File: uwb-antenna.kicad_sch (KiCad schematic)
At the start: 19 parts, among them J1 USB_C_Receptacle_USB2.0_14P, SW1 NRST, SW2 SW_DIP_x02, U1 STM32F401CBUx, Y1 8MHz, Y2 32.768KHz

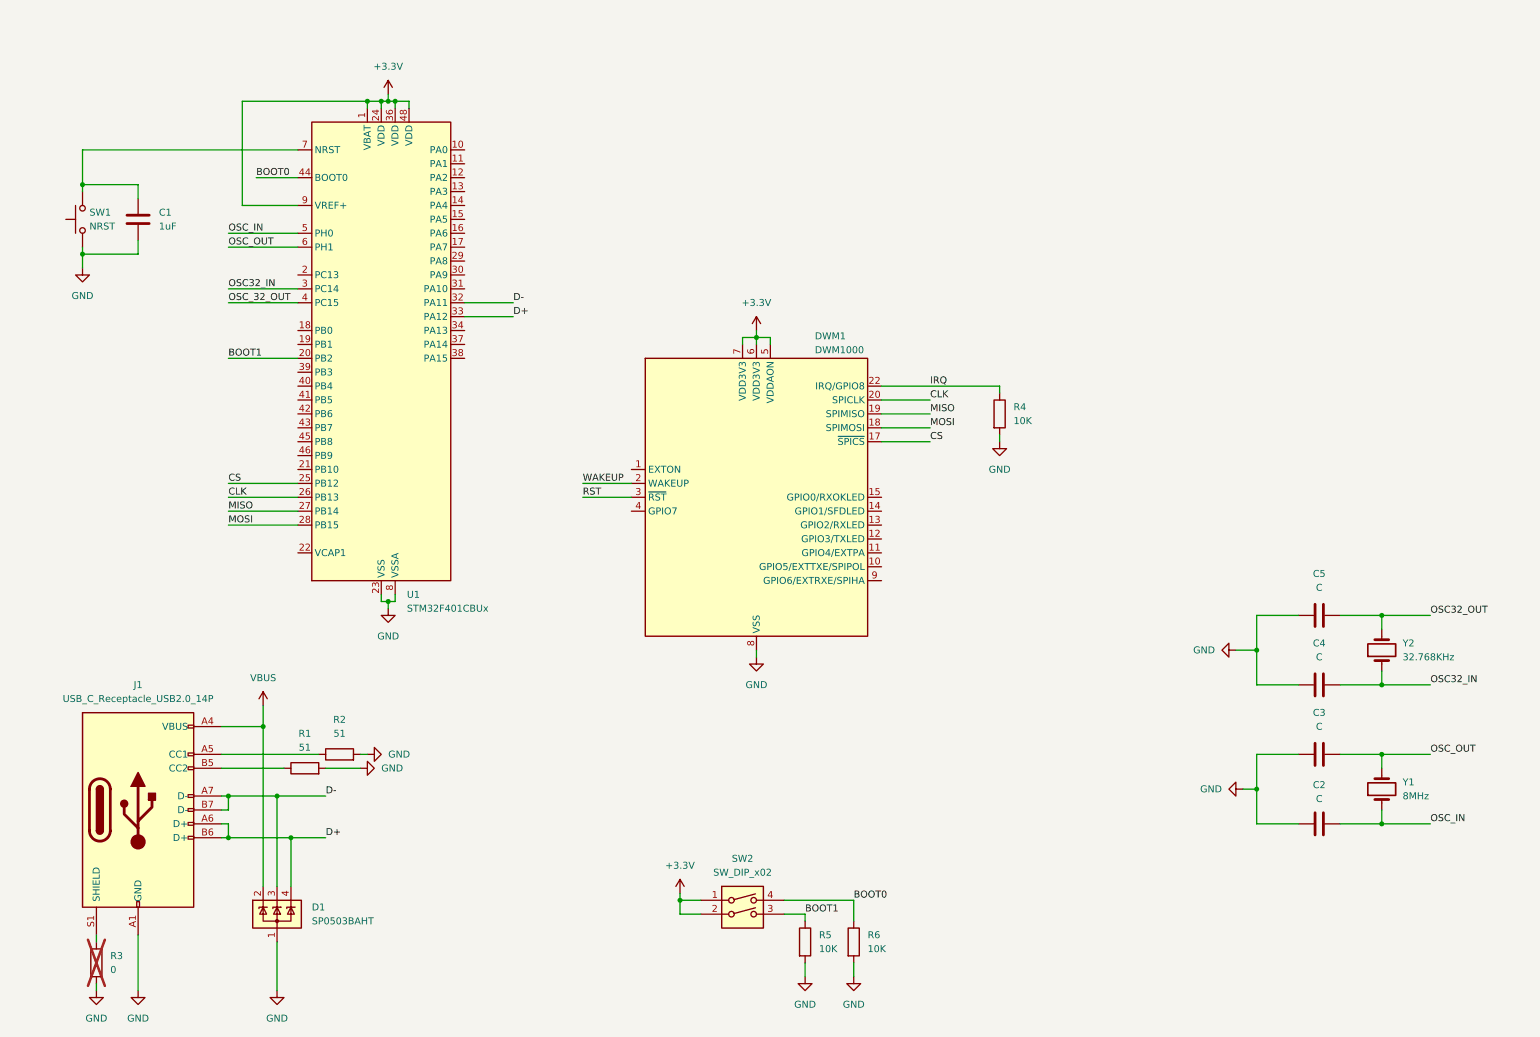
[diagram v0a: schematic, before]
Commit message: feat: add battery charger
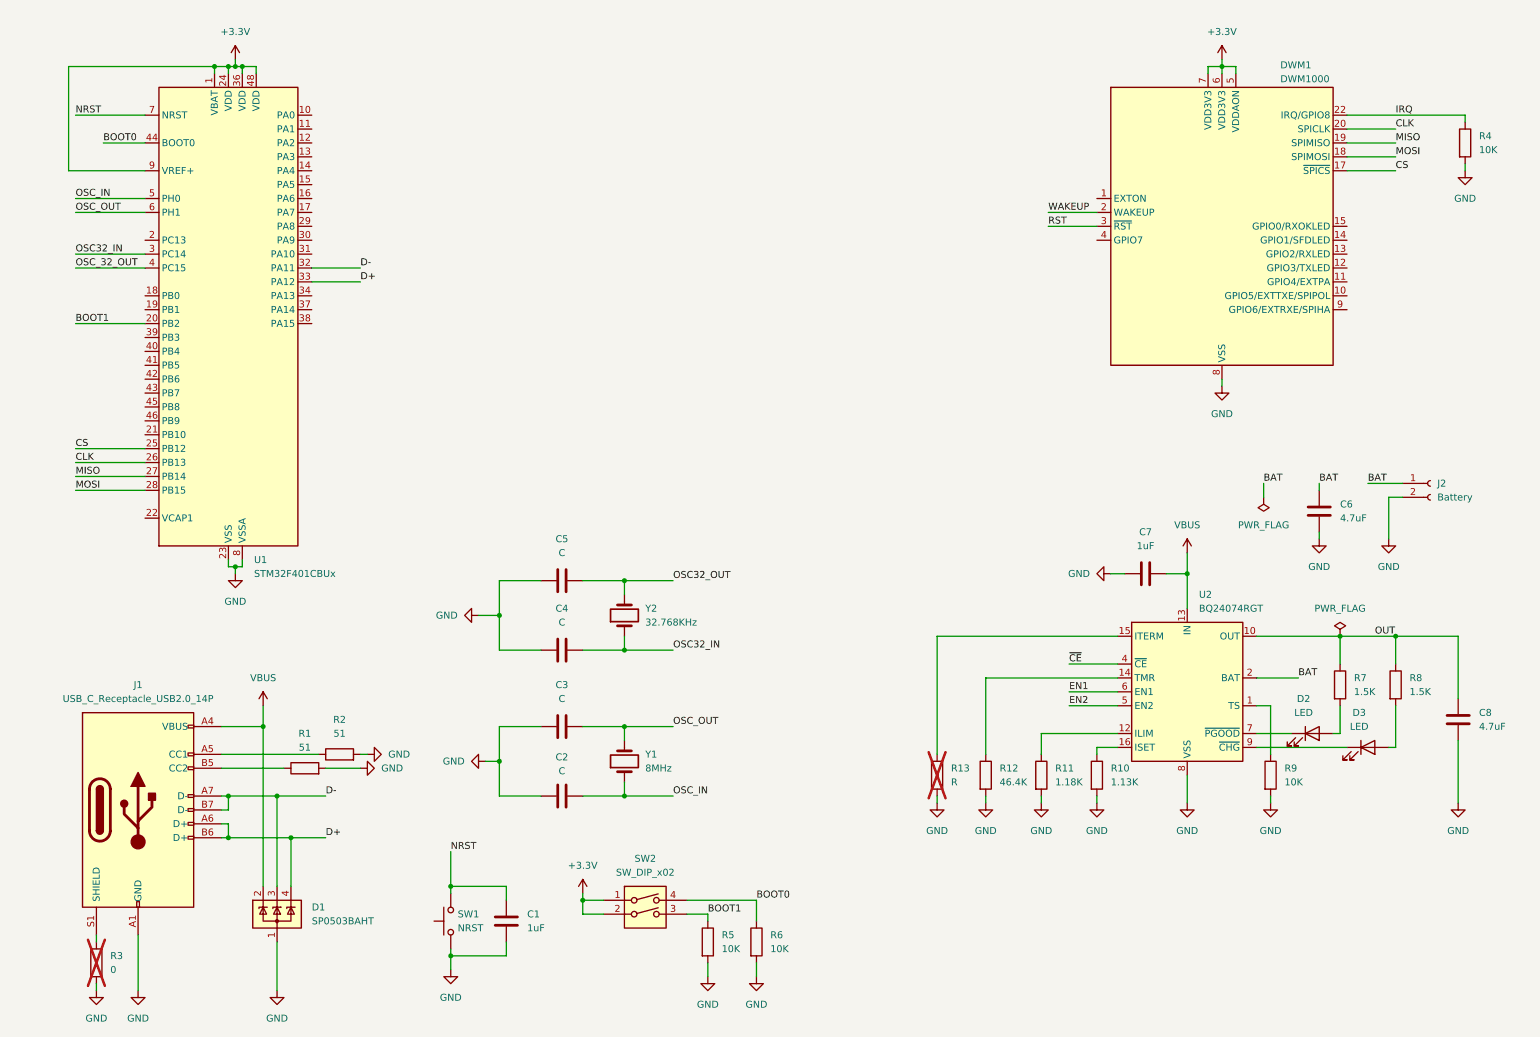
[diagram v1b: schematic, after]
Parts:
- added C6, C8: 4.7uF, symbol Device:C
- added C7: 1uF, symbol Device:C
- added D2, D3: LED, symbol Device:LED
- added J2: Battery, symbol Connector:Conn_01x02_Socket
- added R10: 1.13K, symbol Device:R
- added R11: 1.18K, symbol Device:R
- added R12: 46.4K, symbol Device:R
- added R13: R, symbol Device:R
- added R7, R8: 1.5K, symbol Device:R
- added R9: 10K, symbol Device:R
- added U2: BQ24074RGT, Package_DFN_QFN:VQFN-16-1EP_3x3mm_P0.5mm_EP1.6x1.6mm, symbol Battery_Management:BQ24074RGT
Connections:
- net GND: now also C6.2, C7.2, C8.2, J2.2 (Pin_2), R10.2, R11.2, R12.2, R13.2, R9.2, U2.17 (VSS), U2.8 (VSS)
- net VBUS: now also C7.1, U2.13 (IN)
- net NRST: now reaches C1.1, SW1.2, U1.7 (NRST)
- new net: R9.1, U2.1 (TS)
- new net: R11.1, U2.12 (ILIM)
- new net: R12.1, U2.14 (TMR)
- new net: R13.1, U2.15 (ITERM)
- new net: R10.1, U2.16 (ISET)
- new net: D2.1 (K), U2.7 (~{PGOOD})
- new net: D3.1 (K), U2.9 (~{CHG})
- new net: D3.2 (A), R8.2
- new net: D2.2 (A), R7.2
- new net BAT: C6.1, J2.1 (Pin_1), U2.2 (BAT), U2.3 (BAT)
- new net EN1: U2.6 (EN1)
- new net EN2: U2.5 (EN2)
- new net OUT: C8.1, R7.1, R8.1, U2.10 (OUT), U2.11 (OUT)
- new net ~{CE}: U2.4 (~{CE})
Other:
- moved on the sheet: C1, C2, C3, C4, C5, DWM1, R4, R5, R6, SW1, SW2, U1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

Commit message: feat: complete schematic
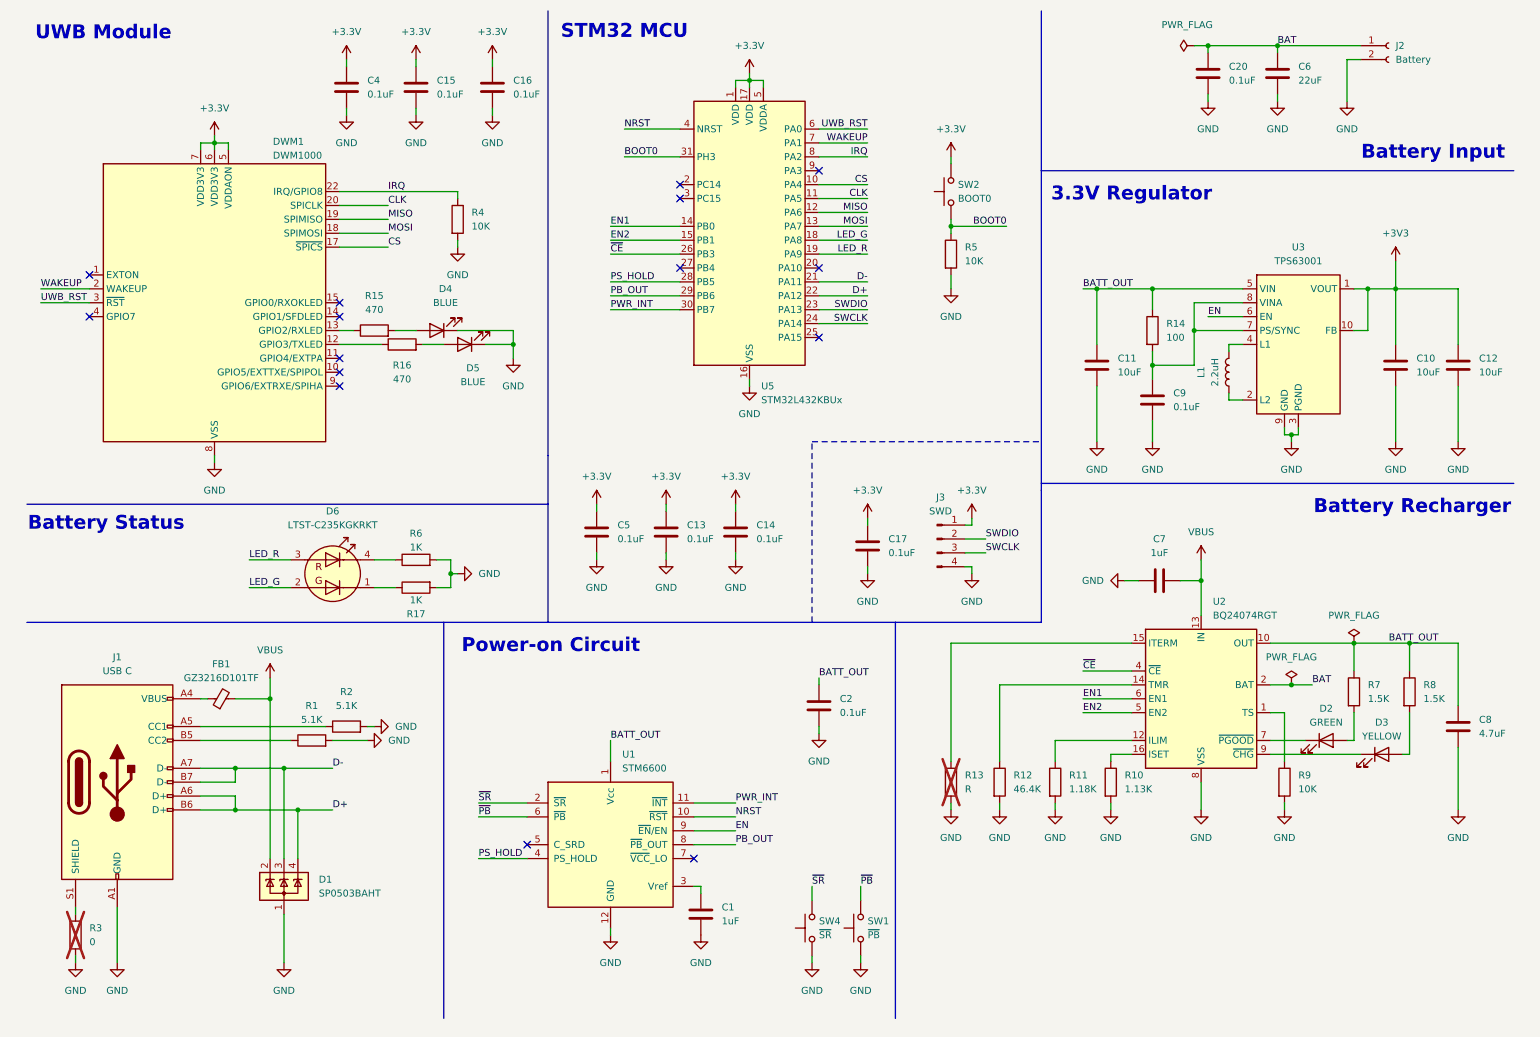
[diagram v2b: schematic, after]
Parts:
- removed C3: C, symbol Device:C
- removed SW2: SW_DIP_x02, symbol Switch:SW_DIP_x02
- removed U1: STM32F401CBUx, Package_DFN_QFN:QFN-48-1EP_7x7mm_P0.5mm_EP5.6x5.6mm, symbol MCU_ST_STM32F4:STM32F401CBUx
- removed Y1: 8MHz, symbol Device:Crystal
- removed Y2: 32.768KHz, symbol Device:Crystal
- added C10, C11, C12: 10uF, Capacitor_SMD:C_0201_0603Metric, symbol Device:C
- added C13, C14, C15, C16, C17: 0.1uF, Capacitor_SMD:C_0402_1005Metric, symbol Device:C
- added C20: 0.1uF, Capacitor_SMD:C_0805_2012Metric, symbol Device:C
- added C9: 0.1uF, Capacitor_SMD:C_0201_0603Metric, symbol Device:C
- added D4, D5: BLUE, LED_SMD:LED_0402_1005Metric, symbol Device:LED
- added D6: LTST-C235KGKRKT, LED_SMD:LED_LiteOn_LTST-C235KGKRKT, symbol LED:LTST-C235KGKRKT
- added FB1: GZ3216D101TF, Inductor_SMD:L_1206_3216Metric, symbol Device:FerriteBead_Small
- added J3: SWD, Connector_PinHeader_2.54mm:PinHeader_1x04_P2.54mm_Vertical, symbol Connector:Conn_01x04_Pin
- added L1: 2.2uH, Inductor_SMD:L_Coilcraft_LPS3010, symbol Device:L
- added R14: 100, Resistor_SMD:R_0201_0603Metric, symbol Device:R
- added R15, R16: 470, Resistor_SMD:R_0402_1005Metric, symbol Device:R
- added R17: 1K, Resistor_SMD:R_0805_2012Metric, symbol Device:R
- added SW2: BOOT0, Button_Switch_SMD:SW_SPST_B3U-1000P, symbol Switch:SW_Push
- added SW4: ~{SR}, Button_Switch_SMD:SW_SPST_B3U-1000P, symbol Switch:SW_Push
- added U1: STM6600, Package_DFN_QFN:TDFN-12_2x3mm_P0.5mm, symbol Power_Management:STM6600
- added U3: TPS63001, Package_SON:Texas_DRC0010J_ThermalVias, symbol Regulator_Switching:TPS63001
- added U5: STM32L432KBUx, Package_DFN_QFN:QFN-32-1EP_5x5mm_P0.5mm_EP3.45x3.45mm, symbol MCU_ST_STM32L4:STM32L432KBUx
- C1: footprint (none) -> Capacitor_SMD:C_0402_1005Metric; LCSC (none) -> C14445
- C2, C4, C5: value C -> 0.1uF; footprint (none) -> Capacitor_SMD:C_0402_1005Metric; LCSC (none) -> C307331
- C6: value 4.7uF -> 22uF; footprint (none) -> Capacitor_SMD:C_1210_3225Metric; LCSC (none) -> C5341638
- C7: footprint (none) -> Capacitor_SMD:C_0402_1005Metric; LCSC (none) -> C105883
- C8: footprint (none) -> Capacitor_SMD:C_0805_2012Metric; LCSC (none) -> C1779
- D1: LCSC (none) -> C41364459
- D2: value LED -> GREEN; footprint (none) -> LED_SMD:LED_0402_1005Metric; LCSC (none) -> C130723
- D3: value LED -> YELLOW; footprint (none) -> LED_SMD:LED_0402_1005Metric; LCSC (none) -> C165978
- J1: value USB_C_Receptacle_USB2.0_14P -> USB C; footprint (none) -> Connector_USB:USB_C_Receptacle_XKB_U262-16XN-4BVC11; LCSC (none) -> C319148
- J2: footprint (none) -> Connector_JST:JST_PH_S2B-PH-K_1x02_P2.00mm_Horizontal
- R1, R2: value 51 -> 5.1K; footprint (none) -> Resistor_SMD:R_0402_1005Metric; LCSC (none) -> C25905
- R10: footprint (none) -> Resistor_SMD:R_0402_1005Metric; LCSC (none) -> C67014
- R11: footprint (none) -> Resistor_SMD:R_0402_1005Metric; LCSC (none) -> C270651
- R12: footprint (none) -> Resistor_SMD:R_0402_1005Metric; LCSC (none) -> C52378
- R13: footprint (none) -> Resistor_SMD:R_0402_1005Metric
- R3: footprint (none) -> Resistor_SMD:R_0805_2012Metric
- R4, R9: footprint (none) -> Resistor_SMD:R_0402_1005Metric; LCSC (none) -> C25744
- R5: footprint (none) -> Resistor_SMD:R_0805_2012Metric; LCSC (none) -> C17414
- R6: value 10K -> 1K; footprint (none) -> Resistor_SMD:R_0805_2012Metric; LCSC (none) -> C17513
- R7, R8: footprint (none) -> Resistor_SMD:R_0402_1005Metric; LCSC (none) -> C25867
- SW1: value NRST -> ~{PB}; footprint (none) -> Button_Switch_SMD:SW_SPST_B3U-1000P; LCSC (none) -> C231329
- U2: LCSC1 (none) -> C54313
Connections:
- net BOOT1 is gone; now on net BOOT0: R5.1
- net OSC32_IN is gone; now on net +3.3V: C4.1
- net OSC32_OUT is gone; now on net +3.3V: C5.1
- net OSC_IN is gone; now on net GND: C2.2
- net +3.3V: now also C13.1, C14.1, C15.1, C16.1, C17.1, J3.1 (Pin_1), SW2.2, U5.1 (VDD), U5.17 (VDD), U5.5 (VDDA)
- net BAT: now also C20.1
- net BOOT0: now also SW2.1, U5.31 (PH3); no longer R6.1
- net CLK: now also U5.11 (PA5)
- net CS: now also U5.10 (PA4)
- net D+: now also U5.22 (PA12)
- net D-: now also U5.21 (PA11)
- net EN1: now also U5.14 (PB0)
- net EN2: now also U5.15 (PB1)
- net GND: now also C10.2, C11.2, C12.2, C13.2, C14.2, C15.2, C16.2, C17.2, C20.2, C9.2, D4.1 (K), D5.1 (K), J3.4 (Pin_4), R17.2, SW4.1, U1.12 (GND), U3.11 (PGND), U3.3 (PGND), U3.9 (GND), U5.16 (VSS), U5.32 (VSS), U5.33 (VSS); no longer C2.1
- net IRQ: now also U5.8 (PA2)
- net MISO: now also U5.12 (PA6)
- net MOSI: now also U5.13 (PA7)
- net NRST: now also U1.10 (~{RST}), U5.4 (NRST); no longer C1.1, SW1.2
- net VBUS: now also FB1.2; no longer J1.A4 (VBUS), J1.A9 (VBUS), J1.B4 (VBUS), J1.B9 (VBUS)
- net WAKEUP: now also U5.7 (PA1)
- net ~{CE}: now also U5.26 (PB3)
- net at DWM1.12 (GPIO3/TXLED): now also R16.1
- net at DWM1.13 (GPIO2/RXLED): now also R15.1
- net OUT renamed BATT_OUT
- net BATT_OUT: now also C2.1, C11.1, R14.1, U1.1 (Vcc), U3.5 (VIN)
- net RST renamed UWB_RST
- net UWB_RST: now also U5.6 (PA0)
- new net: C1.1, U1.3 (Vref)
- new net: D6.1 (K2), R17.1
- new net: D6.4 (K1), R6.1
- new net: C9.1, R14.2, U3.7 (PS/SYNC), U3.8 (VINA)
- new net: D4.2 (A), R15.2
- new net: L1.1, U3.2 (L2)
- new net: L1.2, U3.4 (L1)
- new net: FB1.1, J1.A4 (VBUS), J1.A9 (VBUS), J1.B4 (VBUS), J1.B9 (VBUS)
- new net: D5.2 (A), R16.2
- new net +3V3: C10.1, C12.1, U3.1 (VOUT), U3.10 (FB)
- new net EN: U1.9 (~{EN}/EN), U3.6 (EN)
- new net LED_G: D6.2 (A2), U5.18 (PA8)
- new net LED_R: D6.3 (A1), U5.19 (PA9)
- new net PB_OUT: U1.8 (~{PB}_OUT), U5.29 (PB6)
- new net PS_HOLD: U1.4 (PS_HOLD), U5.28 (PB5)
- new net PWR_INT: U1.11 (~{INT}), U5.30 (PB7)
- new net SWCLK: J3.3 (Pin_3), U5.24 (PA14)
- new net SWDIO: J3.2 (Pin_2), U5.23 (PA13)
- new net ~{PB}: SW1.2, U1.6 (~{PB})
- new net ~{SR}: SW4.2, U1.2 (~{SR})
- no-connect marks 0 -> 15
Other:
- note added: "3.3V Regulator"
- note added: "Battery Input"
- note added: "Battery Recharger"
- note added: "Battery Status"
- note added: "Power-on Circuit"
- note added: "STM32 MCU"
- note added: "UWB Module"
- company: (none) -> Nicolas Farabegoli
- title: (none) -> UWB Anchor
- moved on the sheet: C6, C7, C8, D1, D2, D3, DWM1, J1, J2, R1, R10, R11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

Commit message: start placing some components in PCB design
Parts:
- removed D6: LTST-C235KGKRKT, LED_SMD:LED_LiteOn_LTST-C235KGKRKT, symbol LED:LTST-C235KGKRKT
- removed J3: SWD, Connector_PinHeader_2.54mm:PinHeader_1x04_P2.54mm_Vertical, symbol Connector:Conn_01x04_Pin
- added C3: 0.1uF, Capacitor_SMD:C_0402_1005Metric, symbol Device:C
- added D7: LED_Dual_AAKK, LED_SMD:LED_LiteOn_LTST-C295K_1.6x0.8mm, symbol Device:LED_Dual_AAKK
- added H1: MH1, MountingHole:MountingHole_3.2mm_M3_Pad, symbol Mechanical:MountingHole
- added H2: MH2, MountingHole:MountingHole_3.2mm_M3_Pad, symbol Mechanical:MountingHole
- added H3: MH3, MountingHole:MountingHole_3.2mm_M3_Pad, symbol Mechanical:MountingHole
- added H4: MH4, MountingHole:MountingHole_3.2mm_M3_Pad, symbol Mechanical:MountingHole
- added J4: Conn_ST_STDC14, Connector_PinHeader_1.27mm:PinHeader_2x07_P1.27mm_Vertical_SMD, symbol Connector:Conn_ST_STDC14
- J2: footprint Connector_JST:JST_PH_S2B-PH-K_1x02_P2.00mm_Horizontal -> Connector_JST:JST_PH_S2B-PH-SM4-TB_1x02-1MP_P2.00mm_Horizontal; LCSC (none) -> C295747
- R17, R6: footprint Resistor_SMD:R_0805_2012Metric -> Resistor_SMD:R_0402_1005Metric; LCSC C17513 -> C11702
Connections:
- net +3.3V: now also J4.3 (VCC)
- net GND: now also C3.2, J4.5 (GND), J4.7 (GND)
- net LED_G: now also D7.2 (A2)
- net LED_R: now also D7.1 (A1)
- net NRST: now also C3.1, J4.12 (~{RST})
- net SWCLK: now also J4.6 (JCLK/SWCLK)
- net SWDIO: now also J4.4 (JTMS/SWDIO)
- net ~{CE}: now also U5.27 (PB4); no longer U5.26 (PB3)
- net at R17.1: now also D7.4 (K2)
- net at R6.1: now also D7.3 (K1)
- new net SWO: J4.8 (JTDO/SWO), U5.26 (PB3)
- no-connect marks 15 -> 19
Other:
- moved on the sheet: C13, C14, C17, C5, R5, SW2, U5

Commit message: feat: place other components in the PCB
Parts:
- added C18: 4.7uF, Capacitor_SMD:C_0805_2012Metric, symbol Device:C
- C7: footprint Capacitor_SMD:C_0402_1005Metric -> Capacitor_SMD:C_0805_2012Metric; LCSC C105883 -> C91185
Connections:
- net BAT: now also C18.1
- net GND: now also C18.2
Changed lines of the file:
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@@
 		)
 	)
+	(wire
+		(pts
+			(xy 250.19 109.22) (xy 250.19 111.76)
+		)
+		(stroke
+			(width 0)
+			(type default)
+		)
+	)
 	(polyline
 		(pts
@@
 		)
 	)
+	(label "BAT"
+		(at 250.19 109.22 0)
+		(effects
+			(font
+				(size 1.27 1.27)
+			)
+			(justify left bottom)
+		)
+	)
 	(label "~{CE}"
 		(at 115.57 59.69 0)
@@
 			)
 		)
-		(property "Footprint" "Capacitor_SMD:C_0402_1005Metric"
+		(property "Footprint" "Capacitor_SMD:C_0805_2012Metric"
 			(at 215.9 117.8052 0)
 			(effects
@@
 			)
 		)
-		(property "LCSC" "C105883"
+		(property "LCSC" "C91185"
 			(at 219.71 116.84 90)
 			(effects
@@
 	)
 	(symbol
+		(lib_id "power:GND")
+		(at 250.19 119.38 0)
+		(unit 1)
+		(exclude_from_sim no)
+		(in_bom yes)
+		(on_board yes)
+		(dnp no)
+		(fields_autoplaced yes)
+		(property "Reference" "#PWR055"
+			(at 250.19 125.73 0)
+			(effects
+				(font
+					(size 1.27 1.27)
+				)
+				(hide yes)
+			)
+		)
+		(property "Value" "GND"
+			(at 250.19 124.46 0)
+			(effects
+				(font
+					(size 1.27 1.27)
+				)
+			)
+		)
+		(property "Footprint" ""
+			(at 250.19 119.38 0)
+			(effects
+				(font
+					(size 1.27 1.27)
+				)
+				(hide yes)
+			)
+		)
+		(property "Datasheet" ""
+			(at 250.19 119.38 0)
+			(effects
+				(font
+					(size 1.27 1.27)
+				)
+				(hide yes)
+			)
+		)
+		(property "Description" "Power symbol creates a global label with name \"GND\" , ground"
+			(at 250.19 119.38 0)
+			(effects
+				(font
+					(size 1.27 1.27)
+				)
+				(hide yes)
+			)
+		)
+		(pin "1"
+		)
+		(instances
+			(project "uwb-antenna"
+				(path "/f7e38ffb-df5d-4aea-a3f5-296732509798"
+					(reference "#PWR055")
+					(unit 1)
+				)
+			)
+		)
+	)
+	(symbol
 		(lib_id "Device:R")
 		(at 210.82 153.67 0)
@@
 					(unit 1)
 				)
+			)
+		)
+	)
+	(symbol
+		(lib_id "Device:C")
+		(at 250.19 115.57 0)
+		(unit 1)
+		(exclude_from_sim no)
+		(in_bom yes)
+		(on_board yes)
+		(dnp no)
+		(fields_autoplaced yes)
+		(property "Reference" "C18"
+			(at 254 114.2999 0)
+			(effects
+				(font
+					(size 1.27 1.27)
+				)
+				(justify left)
+			)
+		)
+		(property "Value" "4.7uF"
+			(at 254 116.8399 0)
+			(effects
+				(font
+					(size 1.27 1.27)
+				)
+				(justify left)
+			)
+		)
+		(property "Footprint" "Capacitor_SMD:C_0805_2012Metric"
+			(at 251.1552 119.38 0)
+			(effects
+				(font
+					(size 1.27 1.27)
+				)
+				(hide yes)
+			)
+		)
+		(property "Datasheet" "~"
+			(at 250.19 115.57 0)
+			(effects
+				(font
+					(size 1.27 1.27)
+				)
+				(hide yes)
+			)
+		)
+		(property "Description" "Unpolarized capacitor"
+			(at 250.19 115.57 0)
+			(effects
+				(font
+					(size 1.27 1.27)
+				)
+				(hide yes)
+			)
+		)
+		(property "LCSC" "C1779"
+			(at 250.19 115.57 0)
+			(effects
+				(font
+					(size 1.27 1.27)
+				)
+				(hide yes)
+			)
+		)
+		(pin "2"
+		)
+		(pin "1"
+		)
+		(instances
+			(project "uwb-antenna"
+				(path "/f7e38ffb-df5d-4aea-a3f5-296732509798"
+					(reference "C18")
+					(unit 1)
+				)
